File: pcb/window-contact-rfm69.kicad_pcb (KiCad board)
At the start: 2 copper layers, 28.2 x 34 mm, 18 parts, among them IC1 ATMEGA328P-A, P1 VCC, P2 TX/RX, P3 RE1, P4 ISP, P5 RE2, P6 AN

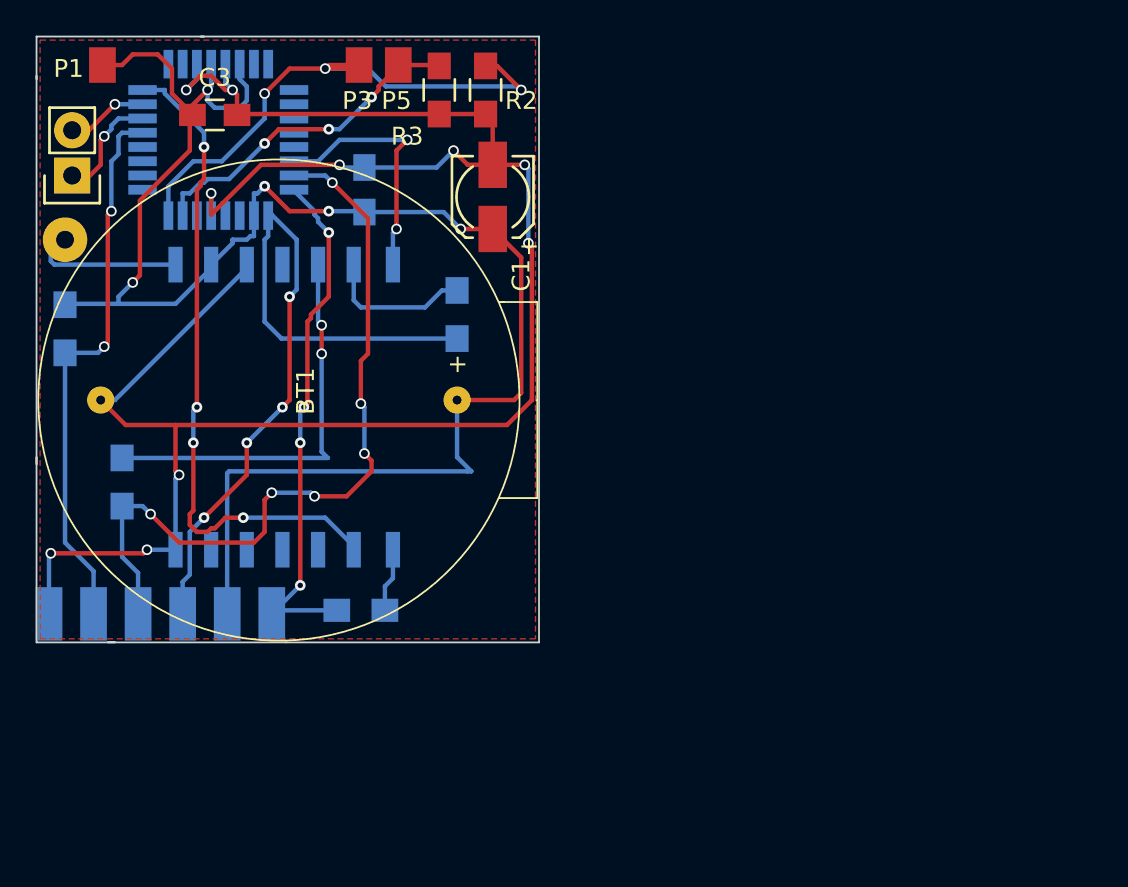
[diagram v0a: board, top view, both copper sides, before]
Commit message: new release of pcb for window four state contact
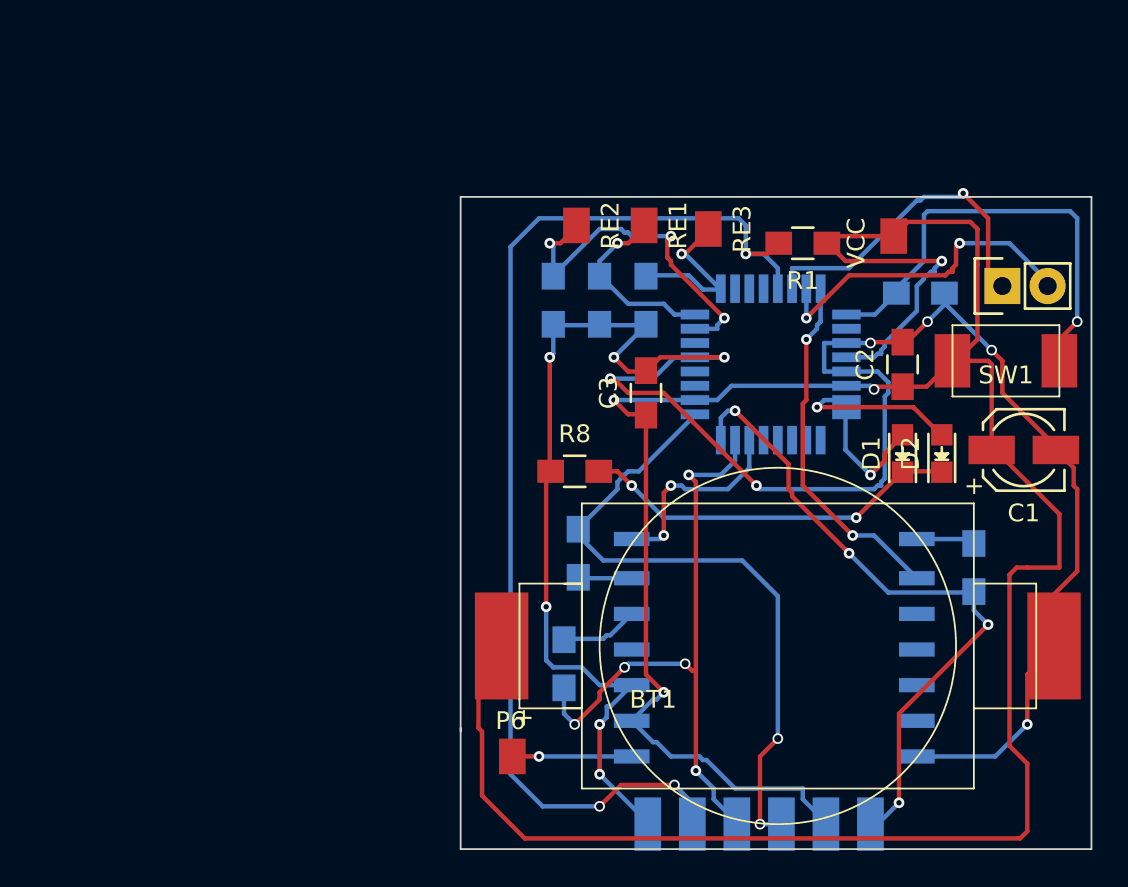
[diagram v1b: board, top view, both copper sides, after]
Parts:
- added D1: RE2, LEDs:LED_0805, F.Cu at (187.2, 137.6)
- added D2: RE1, LEDs:LED_0805, F.Cu at (189.4, 137.6)
- added P7: RE3, wirepad:Wire_SMD_Pad_1PIN, F.Cu at (175.2, 123.4)
- added R7: 10M, Resistors_SMD:R_0805_HandSoldering, B.Cu at (172.8, 129.0)
- added R8: 100, Resistors_SMD:R_0805_HandSoldering, F.Cu at (168.8, 138.6)
- added R9: 10M, Resistors_SMD:R_0805_HandSoldering, B.Cu at (188.2, 128.6)
- added SW1: LED ON, button:SMD_Button, F.Cu at (195.0, 135.4)
- BT1: value CR2477 -> CR2032; footprint battery:CR2477 -> battery:CR2032
- C2, R1: moved to F.Cu
- P6: footprint Wire_Pads:SolderWirePad_single_1mmDrill -> wirepad:Wire_SMD_Pad_1PIN
- R2, R3: moved to B.Cu
- moved P2 52.6 mm to (192.8, 128.2), turned to 90 degrees
- moved P1 45.4 mm to (185.6, 123.8)
- moved R1 41.7 mm to (181.6, 125.8), turned to 180 degrees
- moved P6 36.4 mm to (164.2, 153.0)
- moved P4 35.6 mm to (189.4, 155.4)
- moved R4 34.5 mm to (191.2, 144.0), turned to 270 degrees
- moved RF1 34.5 mm to (188.0, 147.2), turned to 180 degrees
- moved IC1 33.5 mm to (179.8, 132.6), turned to 180 degrees
- moved C1 33.0 mm to (194.0, 137.4), turned to 0 degrees
- moved C2 31.8 mm to (187.2, 132.6)
- moved C3 28.8 mm to (172.8, 134.2), turned to 90 degrees
- moved BT1 27.4 mm to (175.2, 149.4), turned to 0 degrees
- moved R6 26.8 mm to (168.2, 149.4)
- moved P3 18.4 mm to (171.6, 123.2)
- moved R5 15.0 mm to (169.0, 143.2), turned to 270 degrees
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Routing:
- net VCC: track 97.6 -> 161.4 mm, vias 5 -> 4
- net Net-(IC1-Pad29): track 31.3 -> 63.7 mm, vias 2 -> 3
- net Net-(IC1-Pad1): track 0.00 -> 25.6 mm, vias 0 -> 1
- net Net-(IC1-Pad24): track 32.7 -> 10.7 mm, vias 3 -> 1
- net Net-(D1-Pad1): track 0.00 -> 21.6 mm, vias 0 -> 2
- net Net-(R6-Pad2): track 22.6 -> 4.43 mm, vias 2 -> 0
- net Net-(IC1-Pad32): track 37.5 -> 20.0 mm, vias 4 -> 2
- net GND: track 114.9 -> 129.4 mm, vias 10 -> 12
- net Net-(IC1-Pad31): track 4.61 -> 18.9 mm, vias 1 -> 2
- net Net-(IC1-Pad30): track 6.21 -> 18.6 mm
- net Net-(IC1-Pad25): track 0.00 -> 9.99 mm, vias 0 -> 1
- net Net-(D2-Pad2): track 0.00 -> 9.53 mm, vias 0 -> 1
- net /MOSI: track 43.9 -> 35.8 mm, vias 6 -> 5
- net /MISO: track 29.7 -> 37.2 mm
- net Net-(D1-Pad2): track 0.00 -> 7.02 mm, vias 0 -> 1
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- removed copper zone on F.Cu, net GND
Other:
- board size 28.2 x 34 mm -> 35.4 x 36.6 mm

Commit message: finial version for allpcb
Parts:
- renumbered P6 to A
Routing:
- net Net-(IC1-Pad30): track 18.6 -> 20.3 mm
- added copper zone on F.Cu, net GND
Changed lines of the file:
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@@
     (links 53)
     (no_connects 0)
-    (area 162.2 122.6 197.8 160)
+    (area 162.349999 123.149999 197.850001 159.850001)
     (thickness 1.6)
     (drawings 5)
-    (tracks 400)
+    (tracks 399)
     (zones 0)
     (modules 25)
@@
     (last_trace_width 0.25)
     (trace_clearance 0.2)
-    (zone_clearance 0.508)
+    (zone_clearance 0.708)
     (zone_45_only no)
     (trace_min 0.2)
@@
     (fp_line (start -6 7) (end -6 -9) (layer F.SilkS) (width 0.1))
     (fp_line (start -6 -9) (end 16 -9) (layer F.SilkS) (width 0.1))
-    (fp_text user + (at -9.25 3) (layer F.SilkS)
+    (fp_text user + (at -10.8 3) (layer F.SilkS)
       (effects (font (size 1 1) (thickness 0.15)))
     )
@@
     (tags "LED 0805 SMD")
     (attr smd)
-    (fp_text reference D1 (at 0 -1.75 90) (layer F.SilkS)
+    (fp_text reference D1 (at 2.4 0.2 180) (layer F.SilkS)
       (effects (font (size 1 1) (thickness 0.15)))
     )
@@
     (tags "LED 0805 SMD")
     (attr smd)
-    (fp_text reference D2 (at 0 -1.75 90) (layer F.SilkS)
+    (fp_text reference D2 (at 2.6 0 180) (layer F.SilkS)
       (effects (font (size 1 1) (thickness 0.15)))
     )
@@
   (module wirepad:Wire_SMD_Pad_1PIN (layer F.Cu)
     (at 164.2 153)
-    (fp_text reference P6 (at 1 -0.4) (layer F.SilkS)
+    (fp_text reference A (at 2.8 2.6) (layer F.SilkS)
       (effects (font (size 1 1) (thickness 0.15)))
     )
@@
     (tags "resistor 0805")
     (attr smd)
-    (fp_text reference R2 (at 0 2.1 270) (layer B.SilkS)
+    (fp_text reference R2 (at 3.4 0.4 270) (layer B.SilkS)
       (effects (font (size 1 1) (thickness 0.15)) (justify mirror))
     )
@@
     (tags "resistor 0805")
     (attr smd)
-    (fp_text reference R3 (at 0 2.1 270) (layer B.SilkS)
+    (fp_text reference R3 (at 1.6 1.6 270) (layer B.SilkS)
       (effects (font (size 1 1) (thickness 0.15)) (justify mirror))
     )
@@
     (tags "resistor 0805")
     (attr smd)
-    (fp_text reference R7 (at 0 2.1 270) (layer B.SilkS)
+    (fp_text reference R7 (at -1.8 -1.8 270) (layer B.SilkS)
       (effects (font (size 1 1) (thickness 0.15)) (justify mirror))
     )
@@
   (segment (start 173.8 142.2) (end 173.6 142.4) (width 0.25) (layer B.Cu) (net 13) (status 80000))
   (segment (start 173.6 142.4) (end 172 142.4) (width 0.25) (layer B.Cu) (net 13) (status 80000))
-  (segment (start 168.2 150.75) (end 168.2 152.2) (width 0.25) (layer B.Cu) (net 14) (status 400000))
+  (segment (start 168.2 150.75) (end 168.2 152.2) (width 0.25) (layer B.Cu) (net 14))
   (segment (start 175.4 149.8) (end 175.6 149.8) (width 0.25) (layer F.Cu) (net 14))
   (segment (start 175 149.4) (end 175.4 149.8) (width 0.25) (layer F.Cu) (net 14))
@@
   (segment (start 187 157.2) (end 185.8 158.4) (width 0.25) (layer B.Cu) (net 15) (status 80000))
   (segment (start 185.8 158.4) (end 185.4 158.4) (width 0.25) (layer B.Cu) (net 15) (status 80000))
-  (segment (start 169 141.85) (end 169 142.2) (width 0.25) (layer B.Cu) (net 16) (status C00000))
-  (segment (start 169 142.2) (end 170.4 143.6) (width 0.25) (layer B.Cu) (net 16) (status 400000))
-  (segment (start 179.2 158.4) (end 180.4 158.4) (width 0.25) (layer B.Cu) (net 16) (status 800000))
+  (segment (start 169 141.85) (end 169 142.2) (width 0.25) (layer B.Cu) (net 16))
+  (segment (start 169 142.2) (end 170.4 143.6) (width 0.25) (layer B.Cu) (net 16))
+  (segment (start 179.2 158.4) (end 180.4 158.4) (width 0.25) (layer B.Cu) (net 16))
   (via (at 179.2 158.4) (size 0.6) (drill 0.4) (layers F.Cu B.Cu) (net 16))
   (segment (start 179.2 154.6) (end 179.2 158.4) (width 0.25) (layer F.Cu) (net 16))
@@
   (segment (start 179.6 126.4) (end 180.2 125.8) (width 0.25) (layer F.Cu) (net 26) (status 80000))
   (segment (start 180.2 125.8) (end 180.25 125.8) (width 0.25) (layer F.Cu) (net 26) (status 80000))
+  (segment (start 181 128.35) (end 181 126.8) (width 0.25) (layer B.Cu) (net 27))
+  (segment (start 193.2 124.4) (end 193.2 127.8) (width 0.25) (layer F.Cu) (net 27))
+  (segment (start 192.6 123.8) (end 193.2 124.4) (width 0.25) (layer F.Cu) (net 27))
+  (segment (start 184.4 123.8) (end 192.6 123.8) (width 0.25) (layer F.Cu) (net 27))
+  (segment (start 184 124.2) (end 184.4 123.8) (width 0.25) (layer F.Cu) (net 27))
+  (via (at 184 124.2) (size 0.6) (drill 0.4) (layers F.Cu B.Cu) (net 27))
+  (segment (start 183.6 124.2) (end 184 124.2) (width 0.25) (layer B.Cu) (net 27))
+  (segment (start 181 126.8) (end 183.6 124.2) (width 0.25) (layer B.Cu) (net 27))
+  (segment (start 193.2 127.8) (end 192.8 128.2) (width 0.25) (layer F.Cu) (net 27))
   (segment (start 192.8 128.2) (end 192 127.4) (width 0.25) (layer F.Cu) (net 27) (status 80000))
-  (segment (start 192 127.4) (end 192 124.4) (width 0.25) (layer F.Cu) (net 27) (status 80000))
-  (segment (start 192 124.4) (end 190.6 123) (width 0.25) (layer F.Cu) (net 27) (status 80000))
-  (via (at 190.6 123) (size 0.6) (layers F.Cu B.Cu) (net 27) (status 80000))
-  (segment (start 190.6 123) (end 190.4 123.2) (width 0.25) (layer B.Cu) (net 27) (status 80000))
-  (segment (start 190.4 123.2) (end 188.4 123.2) (width 0.25) (layer B.Cu) (net 27) (status 80000))
-  (segment (start 188.4 123.2) (end 188.2 123.4) (width 0.25) (layer B.Cu) (net 27) (status 80000))
-  (segment (start 188.2 123.4) (end 188 123.4) (width 0.25) (layer B.Cu) (net 27) (status 80000))
-  (segment (start 188 123.4) (end 184.2 127.2) (width 0.25) (layer B.Cu) (net 27) (status 80000))
-  (segment (start 184.2 127.2) (end 181 127.2) (width 0.25) (layer B.Cu) (net 27) (status 80000))
-  (segment (start 181 127.2) (end 181 128.35) (width 0.25) (layer B.Cu) (net 27) (status 80000))
   (segment (start 195.34 128.2) (end 195.4 128.2) (width 0.25) (layer B.Cu) (net 28) (status 80000))
   (segment (start 195.4 128.2) (end 195.4 128) (width 0.25) (layer B.Cu) (net 28) (status 80000))
@@
   (segment (start 170.4 148) (end 168.2 148) (width 0.25) (layer B.Cu) (net 33) (status 80000))
   (segment (start 168.2 148) (end 168.2 148.05) (width 0.25) (layer B.Cu) (net 33) (status 80000))
+  (zone (net 2) (net_name GND) (layer F.Cu) (hatch edge 0.508)
+    (connect_pads (clearance 0.708))
+    (min_thickness 0.254)
+    (fill yes (arc_segments 16) (thermal_gap 0.508) (thermal_bridge_width 0.508))
+    (polygon
+      (pts
+        (xy 162.8 123.6) (xy 197.4 123.6) (xy 197.6 159.6) (xy 162.6 159.6) (xy 162.8 158.4)
+      )
+    )
+  )
 )
